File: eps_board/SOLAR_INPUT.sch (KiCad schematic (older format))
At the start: 1 part

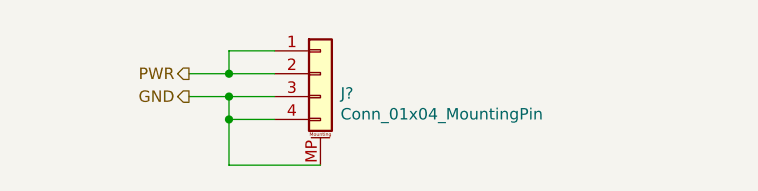
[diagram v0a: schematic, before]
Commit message: EPS with schottky diodes & 1 regulator
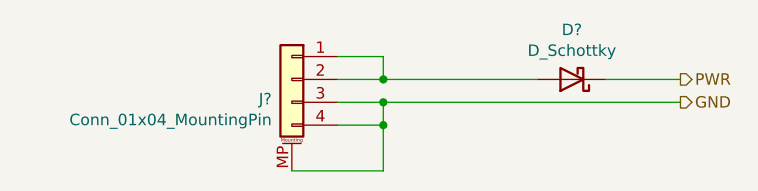
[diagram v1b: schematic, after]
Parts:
- added D?: D_Schottky, footprint_custom:D_SOD-123FL_handsolder, symbol Device:D_Schottky
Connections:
- net PWR: now also D?.1 (K); no longer J?.1 (Pin_1), J?.2 (Pin_2)
- new net: D?.2 (A), J?.1 (Pin_1), J?.2 (Pin_2)
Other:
- moved on the sheet: J?
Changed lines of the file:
@@
 $Descr A 11000 8500
 encoding utf-8
-Sheet 3 21
+Sheet 2 14
 Title "SOLAR CELL INPUT"
 Date "2020-08-09"
@@
 Comment4 ""
 $EndDescr
-Text HLabel 4950 3750 0    50   Output ~ 0
+Text HLabel 7100 3775 2    50   Output ~ 0
 PWR
-Text HLabel 4950 3850 0    50   Output ~ 0
+Text HLabel 7100 3875 2    50   Output ~ 0
 GND
 Wire Wire Line
-	4950 3750 5125 3750
-Wire Wire Line
-	4950 3850 5125 3850
+	7100 3875 5800 3875
 $Comp
 L Connector_Generic_MountingPin:Conn_01x04_MountingPin J?
 U 1 1 5F353115
-P 5525 3750
+P 5400 3775
 AR Path="/5F301B61/5F353115" Ref="J?"  Part="1"
 AR Path="/5F354B90/5F353115" Ref="J?"  Part="1"
@@
 AR Path="/5F3BED82/5F353115" Ref="J?"  Part="1"
 AR Path="/5F3C01C1/5F353115" Ref="J?"  Part="1"
-F 0 "J?" H 5613 3664 50  0000 L CNN
-F 1 "Conn_01x04_MountingPin" H 5613 3573 50  0000 L CNN
-F 2 "Connector_Molex:Molex_Pico-Lock_504050-0491_1x04-1MP_P1.50mm_Horizontal" H 5525 3750 50  0001 C CNN
-F 3 "~" H 5525 3750 50  0001 C CNN
-	1    5525 3750
-	1    0    0    -1
+F 0 "J?" H 5488 3689 50  0000 L CNN
+F 1 "Conn_01x04_MountingPin" H 5488 3598 50  0000 L CNN
+F 2 "Connector_Molex:Molex_Pico-Lock_504050-0491_1x04-1MP_P1.50mm_Horizontal" H 5400 3775 50  0001 C CNN
+F 3 "~" H 5400 3775 50  0001 C CNN
+	1    5400 3775
+	-1   0    0    -1
 $EndComp
 Wire Wire Line
-	5125 3850 5125 3950
+	5800 3875 5800 3975
 Wire Wire Line
-	5125 3950 5325 3950
-Connection ~ 5125 3850
+	5800 3975 5600 3975
+Connection ~ 5800 3875
 Wire Wire Line
-	5125 3850 5325 3850
+	5800 3875 5600 3875
 Wire Wire Line
-	5125 3750 5125 3650
+	5800 3775 5800 3675
 Wire Wire Line
-	5125 3650 5325 3650
-Connection ~ 5125 3750
+	5800 3675 5600 3675
+Connection ~ 5800 3775
 Wire Wire Line
-	5125 3750 5325 3750
+	5800 3775 5600 3775
 Wire Wire Line
-	5125 3950 5125 4150
+	5800 3975 5800 4175
 Wire Wire Line
-	5125 4150 5525 4150
-Connection ~ 5125 3950
+	5800 4175 5400 4175
+Connection ~ 5800 3975
+$Comp
+L Device:D_Schottky D?
+U 1 1 5F649DDE
+P 6625 3775
+AR Path="/5F649DDE" Ref="D?"  Part="1"
+AR Path="/5F301B61/5F649DDE" Ref="D?"  Part="1"
+AR Path="/5F3BB61D/5F649DDE" Ref="D?"  Part="1"
+F 0 "D?" H 6625 3558 50  0000 C CNN
+F 1 "D_Schottky" H 6625 3649 50  0000 C CNN
+F 2 "footprint_custom:D_SOD-123FL_handsolder" H 6625 3775 50  0001 C CNN
+F 3 "https://www.onsemi.com/pub/Collateral/MBR120VLSFT1-D.PDF" H 6625 3775 50  0001 C CNN
+F 4 "NRVB120VLSFT1G" H 6625 3775 50  0001 C CNN "Mfr. #"
+F 5 "https://www.digikey.com/product-detail/en/on-semiconductor/NRVB120VLSFT1G/NRVB120VLSFT1GOSCT-ND/8538727" H 6625 3775 50  0001 C CNN "Order"
+	1    6625 3775
+	-1   0    0    1
+$EndComp
+Wire Wire Line
+	5800 3775 6475 3775
+Wire Wire Line
+	6775 3775 7100 3775
 $EndSCHEMATC

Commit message: Progress on EPS
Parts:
- added R? (x2): 100k, Resistor_SMD:R_0603_1608Metric_Pad1.05x0.95mm_HandSolder, symbol Device:R
- D?: value D_Schottky -> NRVB120VLSFT1G
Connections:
- net GND: now also R?.2
- net at D?.2 (A), J?.1 (Pin_1), J?.2 (Pin_2): now also R?.1
- new net ADC: R?.1, R?.2
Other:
- note added: "NRVB120VLSFT1G"

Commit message: Essentially done with EPS schematic
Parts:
- J1: renamed from J?; Mfr. # (none) -> 5040500491; Order (none) -> https://www.digikey.com/en/products/detail/molex/5040500491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
- R59, R60: renamed from R?; value 100k -> 100K; Mfr. # (none) -> RMCF0603FT100K; Order (none) -> https://www.digikey.com/en/products/detail/stackpole-electr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
- gave numbers to parts that had none: 1
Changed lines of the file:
@@
 $Descr A 11000 8500
 encoding utf-8
-Sheet 36 39
+Sheet 37 39
 Title "Solar Input"
 Date "2020-08-09"
@@
 GND
 $Comp
-L Connector_Generic_MountingPin:Conn_01x04_MountingPin J?
+L Connector_Generic_MountingPin:Conn_01x04_MountingPin J1
 U 1 1 5F353115
 P 5400 3775
-AR Path="/5F301B61/5F353115" Ref="J?"  Part="1"
+AR Path="/5F301B61/5F353115" Ref="J1"  Part="1"
 AR Path="/5F354B90/5F353115" Ref="J?"  Part="1"
 AR Path="/5F354E2E/5F353115" Ref="J?"  Part="1"
@@
 AR Path="/5F3BED82/5F353115" Ref="J?"  Part="1"
 AR Path="/5F3C01C1/5F353115" Ref="J?"  Part="1"
-AR Path="/61651505/5F353115" Ref="J?"  Part="1"
-AR Path="/6165EBE4/5F353115" Ref="J?"  Part="1"
-AR Path="/6166C2BB/5F353115" Ref="J?"  Part="1"
-AR Path="/61679A36/5F353115" Ref="J?"  Part="1"
-AR Path="/616870B5/5F353115" Ref="J?"  Part="1"
-F 0 "J?" H 5488 3689 50  0000 L CNN
+AR Path="/61651505/5F353115" Ref="J7"  Part="1"
+AR Path="/6165EBE4/5F353115" Ref="J8"  Part="1"
+AR Path="/6166C2BB/5F353115" Ref="J9"  Part="1"
+AR Path="/61679A36/5F353115" Ref="J10"  Part="1"
+AR Path="/616870B5/5F353115" Ref="J11"  Part="1"
+F 0 "J11" H 5488 3689 50  0000 L CNN
 F 1 "Conn_01x04_MountingPin" H 5488 3598 50  0000 L CNN
 F 2 "Connector_Molex:Molex_Pico-Lock_504050-0491_1x04-1MP_P1.50mm_Horizontal" H 5400 3775 50  0001 C CNN
 F 3 "~" H 5400 3775 50  0001 C CNN
+F 4 "5040500491" H 5400 3775 50  0001 C CNN "Mfr. #"
+F 5 "https://www.digikey.com/en/products/detail/molex/5040500491/4357649" H 5400 3775 50  0001 C CNN "Order"
 	1    5400 3775
 	-1   0    0    -1
@@
 P 6625 3775
 AR Path="/5F649DDE" Ref="D?"  Part="1"
-AR Path="/5F301B61/5F649DDE" Ref="D?"  Part="1"
+AR Path="/5F301B61/5F649DDE" Ref="D10"  Part="1"
 AR Path="/5F3BB61D/5F649DDE" Ref="D?"  Part="1"
 AR Path="/5F3BED82/5F649DDE" Ref="D?"  Part="1"
@@
 AR Path="/5F3BC7D4/5F649DDE" Ref="D?"  Part="1"
 AR Path="/5F3C01C1/5F649DDE" Ref="D?"  Part="1"
-AR Path="/61651505/5F649DDE" Ref="D?"  Part="1"
-AR Path="/6165EBE4/5F649DDE" Ref="D?"  Part="1"
-AR Path="/6166C2BB/5F649DDE" Ref="D?"  Part="1"
-AR Path="/61679A36/5F649DDE" Ref="D?"  Part="1"
-AR Path="/616870B5/5F649DDE" Ref="D?"  Part="1"
-F 0 "D?" H 6625 3558 50  0000 C CNN
+AR Path="/61651505/5F649DDE" Ref="D13"  Part="1"
+AR Path="/6165EBE4/5F649DDE" Ref="D14"  Part="1"
+AR Path="/6166C2BB/5F649DDE" Ref="D15"  Part="1"
+AR Path="/61679A36/5F649DDE" Ref="D16"  Part="1"
+AR Path="/616870B5/5F649DDE" Ref="D17"  Part="1"
+F 0 "D17" H 6625 3558 50  0000 C CNN
 F 1 "NRVB120VLSFT1G" H 6625 3649 50  0000 C CNN
 F 2 "footprint_custom:D_SOD-123FL_handsolder" H 6625 3775 50  0001 C CNN
@@
 AR Path="/5F5C3BDB/61641278" Ref="R?"  Part="1"
 AR Path="/5F62C305/61641278" Ref="R?"  Part="1"
-AR Path="/5F301B61/61641278" Ref="R?"  Part="1"
-AR Path="/61651505/61641278" Ref="R?"  Part="1"
-AR Path="/6165EBE4/61641278" Ref="R?"  Part="1"
-AR Path="/6166C2BB/61641278" Ref="R?"  Part="1"
-AR Path="/61679A36/61641278" Ref="R?"  Part="1"
-AR Path="/616870B5/61641278" Ref="R?"  Part="1"
-F 0 "R?" H 6350 4400 50  0000 C CNN
-F 1 "100k" H 6400 4525 50  0000 C CNN
+AR Path="/5F301B61/61641278" Ref="R60"  Part="1"
+AR Path="/61651505/61641278" Ref="R307"  Part="1"
+AR Path="/6165EBE4/61641278" Ref="R309"  Part="1"
+AR Path="/6166C2BB/61641278" Ref="R311"  Part="1"
+AR Path="/61679A36/61641278" Ref="R313"  Part="1"
+AR Path="/616870B5/61641278" Ref="R315"  Part="1"
+F 0 "R315" H 6400 4400 50  0000 C CNN
+F 1 "100K" H 6400 4525 50  0000 C CNN
 F 2 "Resistor_SMD:R_0603_1608Metric_Pad1.05x0.95mm_HandSolder" V 6180 4450 50  0001 C CNN
 F 3 "~" H 6250 4450 50  0001 C CNN
+F 4 "RMCF0603FT100K" H 6250 4450 50  0001 C CNN "Mfr. #"
+F 5 "https://www.digikey.com/en/products/detail/stackpole-electronics-inc/RMCF0603FT100K/1761112" H 6250 4450 50  0001 C CNN "Order"
 	1    6250 4450
 	1    0    0    -1
@@
 AR Path="/5F5C3BDB/61694927" Ref="R?"  Part="1"
 AR Path="/5F62C305/61694927" Ref="R?"  Part="1"
-AR Path="/5F301B61/61694927" Ref="R?"  Part="1"
-AR Path="/61651505/61694927" Ref="R?"  Part="1"
-AR Path="/6165EBE4/61694927" Ref="R?"  Part="1"
-AR Path="/6166C2BB/61694927" Ref="R?"  Part="1"
-AR Path="/61679A36/61694927" Ref="R?"  Part="1"
-AR Path="/616870B5/61694927" Ref="R?"  Part="1"
-F 0 "R?" H 6350 3950 50  0000 C CNN
-F 1 "100k" H 6400 4075 50  0000 C CNN
+AR Path="/5F301B61/61694927" Ref="R59"  Part="1"
+AR Path="/61651505/61694927" Ref="R306"  Part="1"
+AR Path="/6165EBE4/61694927" Ref="R308"  Part="1"
+AR Path="/6166C2BB/61694927" Ref="R310"  Part="1"
+AR Path="/61679A36/61694927" Ref="R312"  Part="1"
+AR Path="/616870B5/61694927" Ref="R314"  Part="1"
+F 0 "R314" H 6400 3950 50  0000 C CNN
+F 1 "100K" H 6400 4075 50  0000 C CNN
 F 2 "Resistor_SMD:R_0603_1608Metric_Pad1.05x0.95mm_HandSolder" V 6180 4000 50  0001 C CNN
 F 3 "~" H 6250 4000 50  0001 C CNN
+F 4 "RMCF0603FT100K" H 6250 4000 50  0001 C CNN "Mfr. #"
+F 5 "https://www.digikey.com/en/products/detail/stackpole-electronics-inc/RMCF0603FT100K/1761112" H 6250 4000 50  0001 C CNN "Order"
 	1    6250 4000
 	1    0    0    -1

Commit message: EPS layout in progress
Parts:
- removed J1: Conn_01x04_MountingPin, Connector_Molex:Molex_Pico-Lock_504050-0491_1x04-1MP_P1.50mm_Horizontal, symbol Connector_Generic_MountingPin:Conn_01x04_MountingPin
- added J5: Conn_01x04, Connector_PinHeader_2.54mm:PinHeader_1x04_P2.54mm_Vertical, symbol Connector_Generic:Conn_01x04
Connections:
- net GND: now also J5.3 (Pin_3), J5.4 (Pin_4)
- net at D10.2 (A), R59.1: now also J5.1 (Pin_1), J5.2 (Pin_2)
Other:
- note added: "I used to use Molex Pico Lock:\n5040500491\nhttps://www.digikey.com/en/products/detail/molex/5040500491/4357649\n"
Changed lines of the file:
@@
 $Descr A 11000 8500
 encoding utf-8
-Sheet 37 39
+Sheet 34 39
 Title "Solar Input"
 Date "2020-08-09"
@@
 Text HLabel 7100 4675 2    50   Output ~ 0
 GND
-$Comp
-L Connector_Generic_MountingPin:Conn_01x04_MountingPin J1
-U 1 1 5F353115
-P 5400 3775
-AR Path="/5F301B61/5F353115" Ref="J1"  Part="1"
-AR Path="/5F354B90/5F353115" Ref="J?"  Part="1"
-AR Path="/5F354E2E/5F353115" Ref="J?"  Part="1"
-AR Path="/5F355300/5F353115" Ref="J?"  Part="1"
-AR Path="/5F35592A/5F353115" Ref="J?"  Part="1"
-AR Path="/5F356474/5F353115" Ref="J?"  Part="1"
-AR Path="/5F3BB61D/5F353115" Ref="J?"  Part="1"
-AR Path="/5F3BC7D4/5F353115" Ref="J?"  Part="1"
-AR Path="/5F3BD959/5F353115" Ref="J?"  Part="1"
-AR Path="/5F3BED82/5F353115" Ref="J?"  Part="1"
-AR Path="/5F3C01C1/5F353115" Ref="J?"  Part="1"
-AR Path="/61651505/5F353115" Ref="J7"  Part="1"
-AR Path="/6165EBE4/5F353115" Ref="J8"  Part="1"
-AR Path="/6166C2BB/5F353115" Ref="J9"  Part="1"
-AR Path="/61679A36/5F353115" Ref="J10"  Part="1"
-AR Path="/616870B5/5F353115" Ref="J11"  Part="1"
-F 0 "J11" H 5488 3689 50  0000 L CNN
-F 1 "Conn_01x04_MountingPin" H 5488 3598 50  0000 L CNN
-F 2 "Connector_Molex:Molex_Pico-Lock_504050-0491_1x04-1MP_P1.50mm_Horizontal" H 5400 3775 50  0001 C CNN
-F 3 "~" H 5400 3775 50  0001 C CNN
-F 4 "5040500491" H 5400 3775 50  0001 C CNN "Mfr. #"
-F 5 "https://www.digikey.com/en/products/detail/molex/5040500491/4357649" H 5400 3775 50  0001 C CNN "Order"
-	1    5400 3775
-	-1   0    0    -1
-$EndComp
 Wire Wire Line
 	5800 3875 5800 3975
@@
 Wire Wire Line
 	5800 3775 5600 3775
-Wire Wire Line
-	5800 3975 5800 4175
-Wire Wire Line
-	5800 4175 5400 4175
 Connection ~ 5800 3975
 $Comp
@@
 AR Path="/61679A36/5F649DDE" Ref="D16"  Part="1"
 AR Path="/616870B5/5F649DDE" Ref="D17"  Part="1"
-F 0 "D17" H 6625 3558 50  0000 C CNN
+F 0 "D14" H 6625 3558 50  0000 C CNN
 F 1 "NRVB120VLSFT1G" H 6625 3649 50  0000 C CNN
 F 2 "footprint_custom:D_SOD-123FL_handsolder" H 6625 3775 50  0001 C CNN
@@
 Text Notes 9000 900  0    50   ~ 0
 NRVB120VLSFT1G
-Connection ~ 5800 4175
 Wire Wire Line
 	6250 3775 6250 3850
@@
 AR Path="/61679A36/61641278" Ref="R313"  Part="1"
 AR Path="/616870B5/61641278" Ref="R315"  Part="1"
-F 0 "R315" H 6400 4400 50  0000 C CNN
+F 0 "R309" H 6400 4400 50  0000 C CNN
 F 1 "100K" H 6400 4525 50  0000 C CNN
 F 2 "Resistor_SMD:R_0603_1608Metric_Pad1.05x0.95mm_HandSolder" V 6180 4450 50  0001 C CNN
@@
 Wire Wire Line
 	6250 4675 7100 4675
-Wire Wire Line
-	5800 4175 5800 4675
 Wire Wire Line
 	6250 4225 7100 4225
@@
 AR Path="/61679A36/61694927" Ref="R312"  Part="1"
 AR Path="/616870B5/61694927" Ref="R314"  Part="1"
-F 0 "R314" H 6400 3950 50  0000 C CNN
+F 0 "R308" H 6400 3950 50  0000 C CNN
 F 1 "100K" H 6400 4075 50  0000 C CNN
 F 2 "Resistor_SMD:R_0603_1608Metric_Pad1.05x0.95mm_HandSolder" V 6180 4000 50  0001 C CNN
@@
 	1    0    0    -1
 $EndComp
+Text Notes 5325 5775 0    50   ~ 0
+I used to use Molex Pico Lock:\n5040500491\nhttps://www.digikey.com/en/products/detail/molex/5040500491/4357649\n
+$Comp
+L Connector_Generic:Conn_01x04 J5
+U 1 1 5FFDDFD5
+P 5400 3775
+AR Path="/6165EBE4/5FFDDFD5" Ref="J5"  Part="1"
+AR Path="/5F301B61/5FFDDFD5" Ref="J1"  Part="1"
+AR Path="/61651505/5FFDDFD5" Ref="J3"  Part="1"
+AR Path="/6166C2BB/5FFDDFD5" Ref="J7"  Part="1"
+AR Path="/61679A36/5FFDDFD5" Ref="J8"  Part="1"
+AR Path="/616870B5/5FFDDFD5" Ref="J9"  Part="1"
+F 0 "J5" H 5318 4092 50  0000 C CNN
+F 1 "Conn_01x04" H 5318 4001 50  0000 C CNN
+F 2 "Connector_PinHeader_2.54mm:PinHeader_1x04_P2.54mm_Vertical" H 5400 3775 50  0001 C CNN
+F 3 "~" H 5400 3775 50  0001 C CNN
+	1    5400 3775
+	-1   0    0    -1
+$EndComp
+Wire Wire Line
+	5800 3975 5800 4675
 $EndSCHEMATC

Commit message: EPS V1.0 Complete
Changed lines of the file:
@@
 AR Path="/61679A36/5F649DDE" Ref="D16"  Part="1"
 AR Path="/616870B5/5F649DDE" Ref="D17"  Part="1"
-F 0 "D14" H 6625 3558 50  0000 C CNN
+F 0 "D17" H 6625 3558 50  0000 C CNN
 F 1 "NRVB120VLSFT1G" H 6625 3649 50  0000 C CNN
 F 2 "footprint_custom:D_SOD-123FL_handsolder" H 6625 3775 50  0001 C CNN
@@
 AR Path="/61679A36/61641278" Ref="R313"  Part="1"
 AR Path="/616870B5/61641278" Ref="R315"  Part="1"
-F 0 "R309" H 6400 4400 50  0000 C CNN
+F 0 "R315" H 6400 4400 50  0000 C CNN
 F 1 "100K" H 6400 4525 50  0000 C CNN
 F 2 "Resistor_SMD:R_0603_1608Metric_Pad1.05x0.95mm_HandSolder" V 6180 4450 50  0001 C CNN
@@
 AR Path="/61679A36/61694927" Ref="R312"  Part="1"
 AR Path="/616870B5/61694927" Ref="R314"  Part="1"
-F 0 "R308" H 6400 3950 50  0000 C CNN
+F 0 "R314" H 6400 3950 50  0000 C CNN
 F 1 "100K" H 6400 4075 50  0000 C CNN
 F 2 "Resistor_SMD:R_0603_1608Metric_Pad1.05x0.95mm_HandSolder" V 6180 4000 50  0001 C CNN
@@
 AR Path="/61679A36/5FFDDFD5" Ref="J8"  Part="1"
 AR Path="/616870B5/5FFDDFD5" Ref="J9"  Part="1"
-F 0 "J5" H 5318 4092 50  0000 C CNN
+F 0 "J9" H 5318 4092 50  0000 C CNN
 F 1 "Conn_01x04" H 5318 4001 50  0000 C CNN
 F 2 "Connector_PinHeader_2.54mm:PinHeader_1x04_P2.54mm_Vertical" H 5400 3775 50  0001 C CNN
